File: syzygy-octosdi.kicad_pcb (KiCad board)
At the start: 4 copper layers, 100 x 50 mm, 211 parts, among them CN1 QTH-020-01-F-D-DP-A, J1 Conn_Coaxial, J2 Conn_Coaxial, J3 Conn_Coaxial, J4 Conn_Coaxial, J5 Conn_Coaxial, J6 Conn_Coaxial, J7 Conn_Coaxial, J8 Conn_Coaxial, J9 Conn_02x03_Odd_Even, U1 LMH0344SQE_NOPB, U10 GS2988-INE3, U11 STM32G031G8Ux, U2 LMH0344SQE_NOPB, U3 LMH0344SQE_NOPB, U4 LMH0344SQE_NOPB, U5 PCAL6416AHF, U6 PCAL6416AHF, U7 GS2988-INE3, U8 GS2988-INE3, U9 GS2988-INE3, X1 SX7DF148_500B20F30DNN

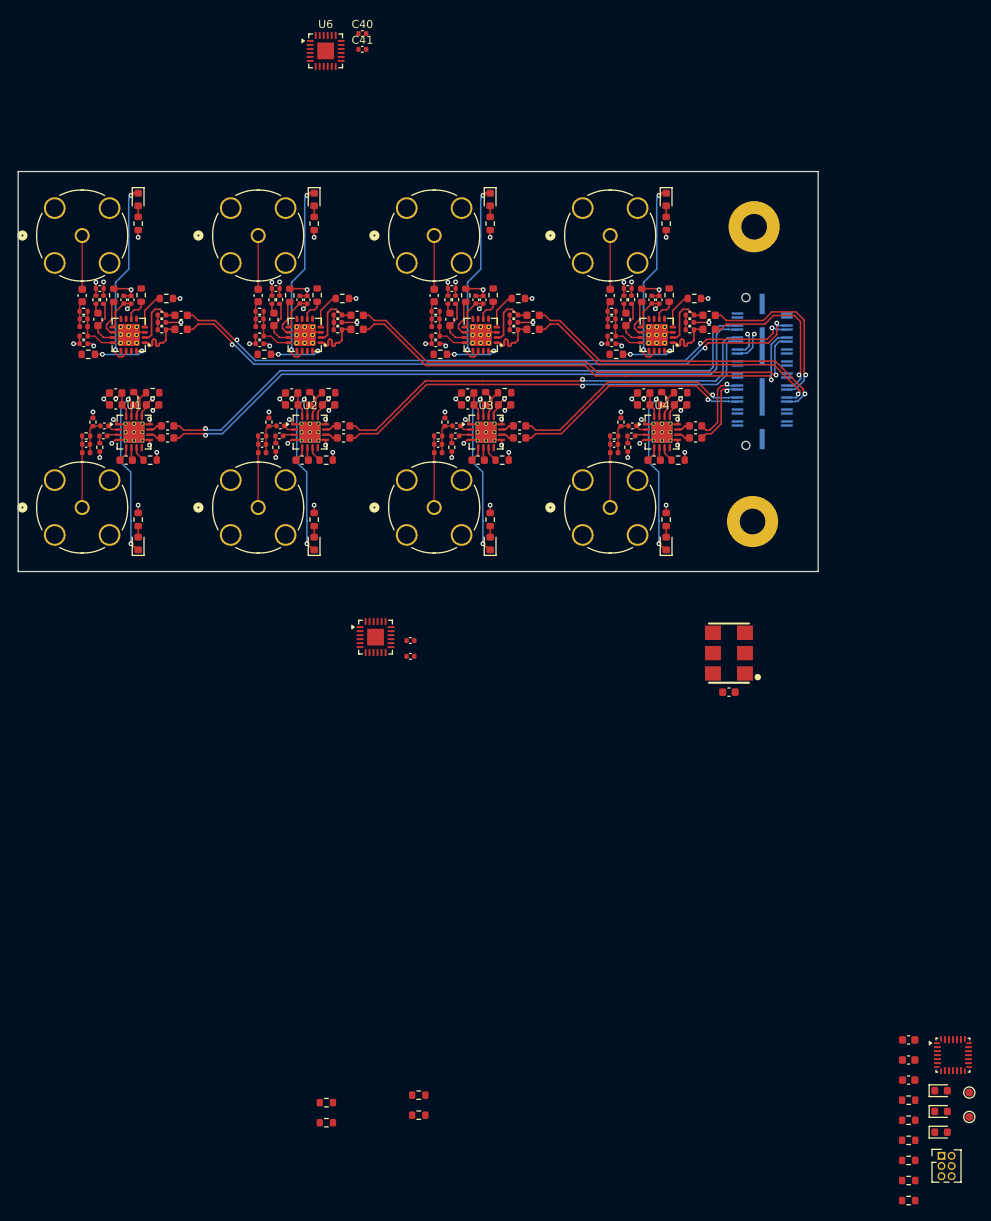
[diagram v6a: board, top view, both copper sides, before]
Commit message: route the smartvio mcu and the gpio expanders
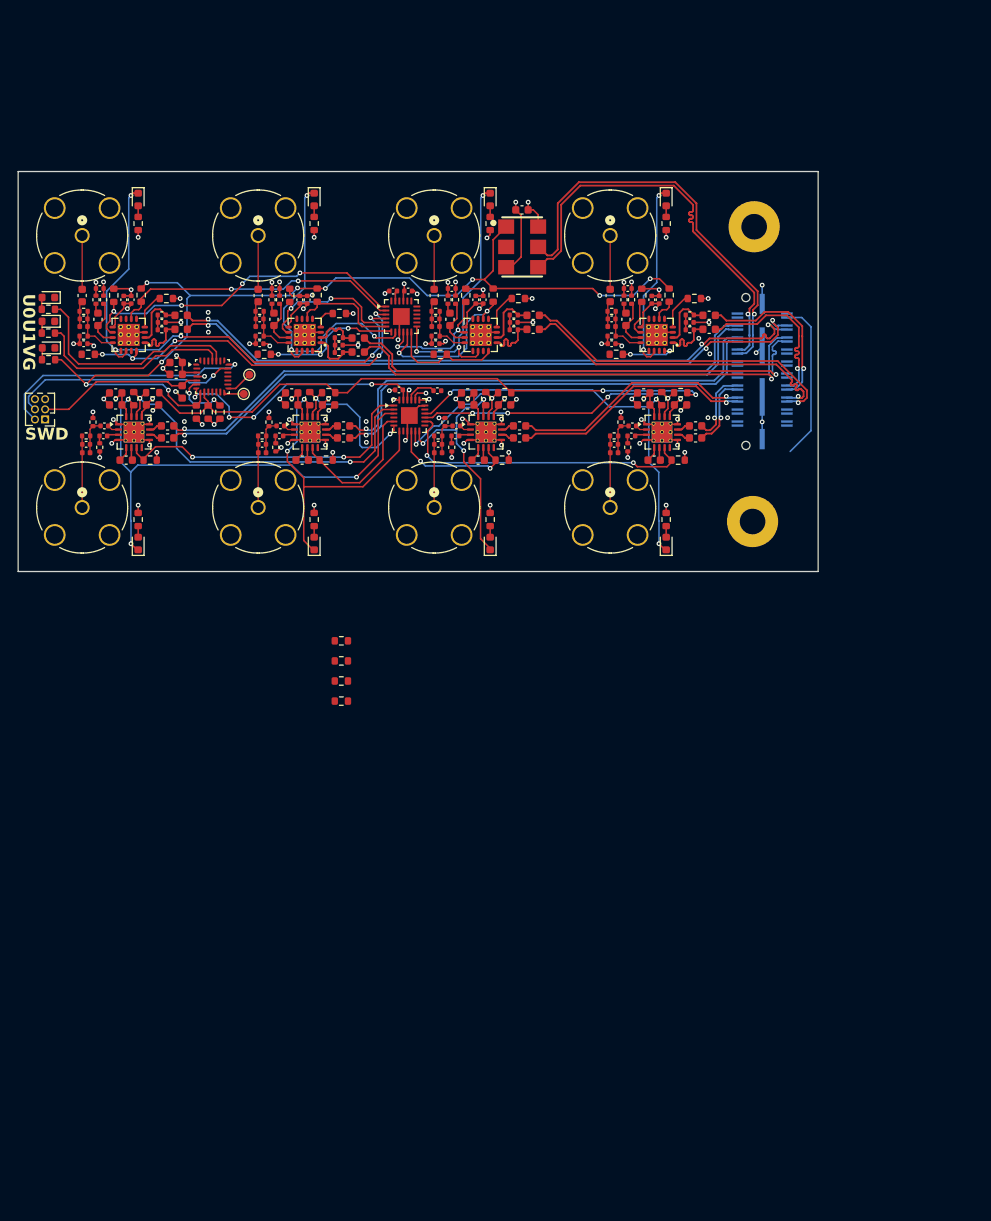
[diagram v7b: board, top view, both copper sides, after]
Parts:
- moved D10 151.0 mm to (53.8, 65.8), turned to 180 degrees
- moved R82 150.4 mm to (53.8, 73.5), turned to 180 degrees
- moved D11 148.5 mm to (53.8, 72.0), turned to 180 degrees
- moved R78 147.8 mm to (53.8, 67.2), turned to 180 degrees
- moved D9 147.3 mm to (53.8, 68.7), turned to 180 degrees
- moved J9 145.0 mm to (53.4, 81.0), turned to 180 degrees
- moved R77 144.1 mm to (53.8, 70.2), turned to 180 degrees
- moved R80 130.0 mm to (73.8, 80.1), turned to 90 degrees
- moved R81 129.1 mm to (72.3, 80.1), turned to -90 degrees
- moved TP2 128.0 mm to (78.2, 77.8)
- moved C84 127.1 mm to (69.8, 75.3), turned to 180 degrees
- moved TP1 127.1 mm to (78.9, 75.4)
- moved C83 126.4 mm to (69.8, 73.9), turned to 180 degrees
- moved U11 125.6 mm to (74.3, 75.6)
- moved R79 125.3 mm to (75.2, 80.1), turned to 90 degrees
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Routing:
- net /VIO_GOOD: track 0.00 -> 122.3 mm, vias 0 -> 9
- net /~{VIO_GOOD}: track 0.00 -> 75.7 mm, vias 0 -> 2
- net /REFCLK.P: track 3.23 -> 52.2 mm
- net /REFCLK.N: track 3.98 -> 52.3 mm
- net /Outputs/SDI Out 1/~{OSP}: track 23.5 -> 66.4 mm, vias 2 -> 5
- net /Inputs/SDI In 1/MUTE: track 4.62 -> 46.6 mm, vias 0 -> 2
- net /Outputs/SDI Out 1/~{EQ_EN}: track 6.72 -> 46.6 mm, vias 2 -> 5
- net /Inputs/SDI In 1/~{CD}: track 22.8 -> 62.5 mm, vias 2 -> 3
- net /Outputs/SDI Out 1/SD/~{HD}: track 4.65 -> 43.1 mm, vias 0 -> 4
- net /Inputs/SDI In 1/BYPASS: track 1.92 -> 39.5 mm, vias 0 -> 2
- net /Inputs/SDI In 4/BYPASS: track 1.92 -> 38.9 mm, vias 0 -> 2
- net GND: track 88.3 -> 123.4 mm, vias 52 -> 75
- net /VIO: track 0.00 -> 33.9 mm, vias 0 -> 4
- net /Outputs/SDI Out 1/~{DISABLE}: track 2.98 -> 36.6 mm, vias 0 -> 2
- net /SmartVIO/SWCLK: track 0.00 -> 32.4 mm, vias 0 -> 1
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- added copper zone on In2.Cu, net GND
- removed copper zone on In2.Cu, net +3V3
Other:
- board text added: "SWD"
- board text added: "U0"
- board text added: "U1"
- board text added: "VG"

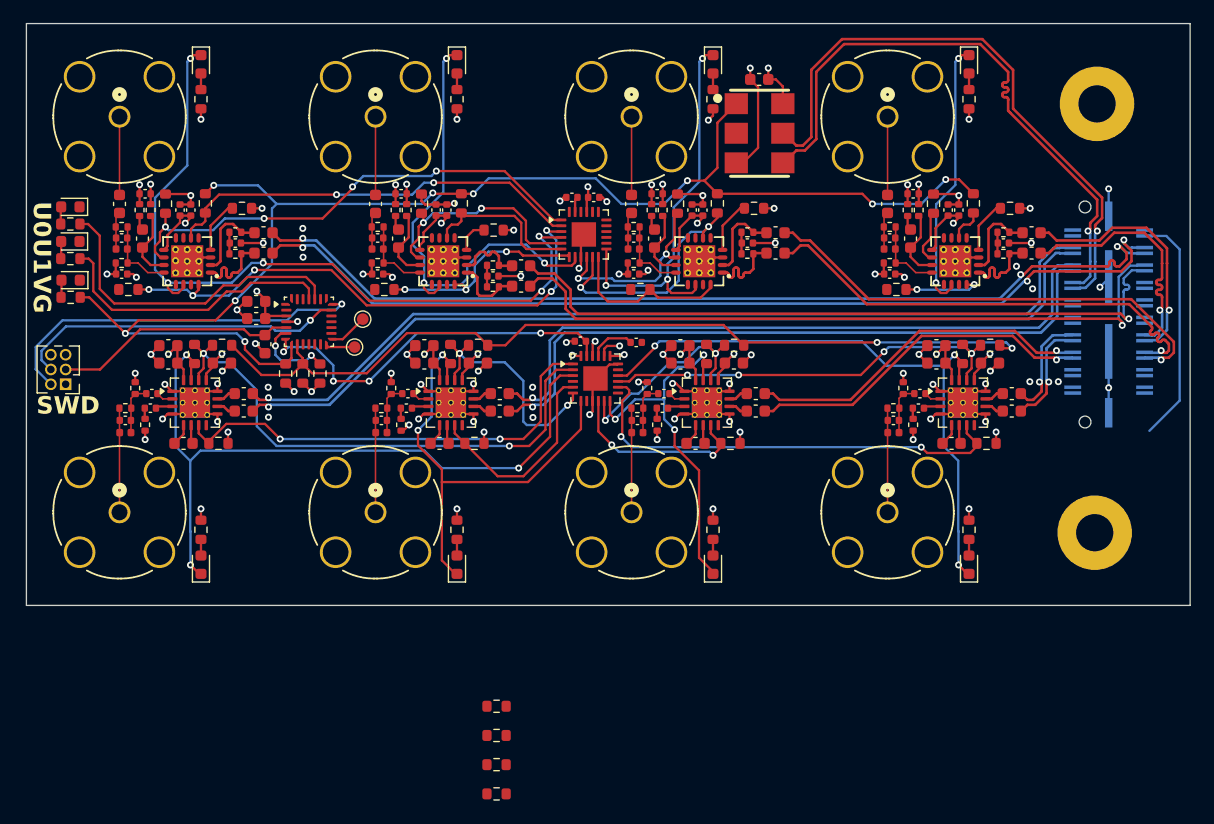
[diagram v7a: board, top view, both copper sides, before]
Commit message: route all the low speed io and start 3v3
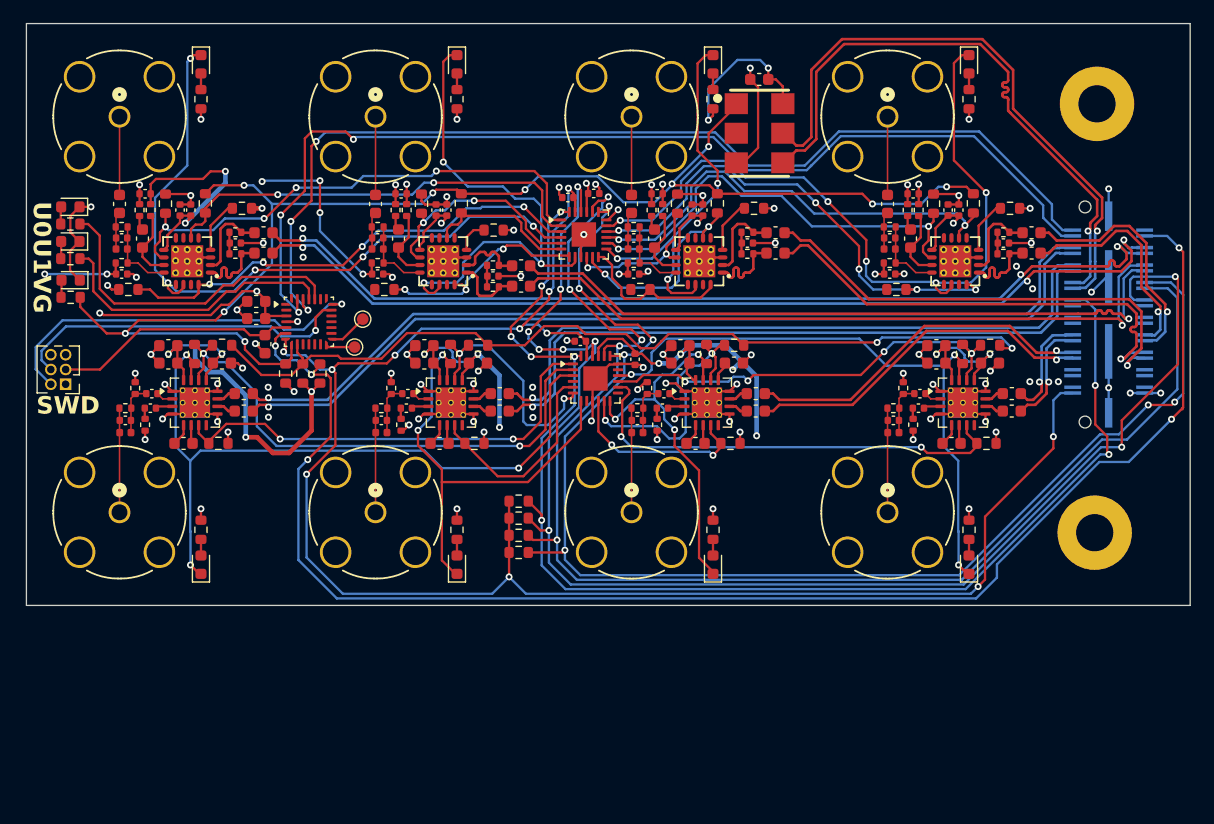
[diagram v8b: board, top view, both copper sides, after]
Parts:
- moved R4 22.3 mm to (92.3, 94.0)
- moved R3 21.3 mm to (92.3, 92.5)
- moved R1 17.7 mm to (92.3, 91.0)
- moved R2 15.8 mm to (92.3, 95.5)
- moved C39 1.45 mm to (102.3, 78.8), turned to -90 degrees
- moved C40 0.35 mm to (96.5, 65.0)
- moved C41 0.34 mm to (98.8, 64.6)
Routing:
- net +3V3: track 91.4 -> 577.3 mm, vias 36 -> 48
- net /~{INT}: track 1.36 -> 126.1 mm, vias 1 -> 9
- net /VIO: track 33.9 -> 152.2 mm, vias 4 -> 11
- net /I2C.SDA: track 2.04 -> 118.9 mm, vias 1 -> 5
- net /I2C.SCL: track 1.27 -> 117.3 mm, vias 1 -> 7
- net /~{RESET}: track 0.78 -> 110.9 mm, vias 1 -> 8
- net /R_GA: track 27.2 -> 128.3 mm, vias 2 -> 5
- net /VIO_I2C.SDA: track 0.00 -> 90.9 mm, vias 0 -> 3
- net /VIO_I2C.SCL: track 0.00 -> 89.2 mm, vias 0 -> 3
- net /Outputs/SDI Out 4/~{OSP}: track 23.5 -> 65.1 mm, vias 2 -> 5
- net /Outputs/SDI Out 4/~{EQ_EN}: track 6.72 -> 42.7 mm, vias 2 -> 5
- net /Outputs/SDI Out 4/~{DISABLE}: track 2.98 -> 38.9 mm, vias 0 -> 2
- net /Outputs/SDI Out 4/SD/~{HD}: track 4.65 -> 38.2 mm, vias 0 -> 2
- net GND: track 123.4 -> 137.2 mm, vias 75 -> 78
- net /Outputs/SDI Out 1/~{EQ_EN}: track 46.6 -> 41.4 mm, vias 5 -> 4
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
